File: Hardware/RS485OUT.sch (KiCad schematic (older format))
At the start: 14 parts

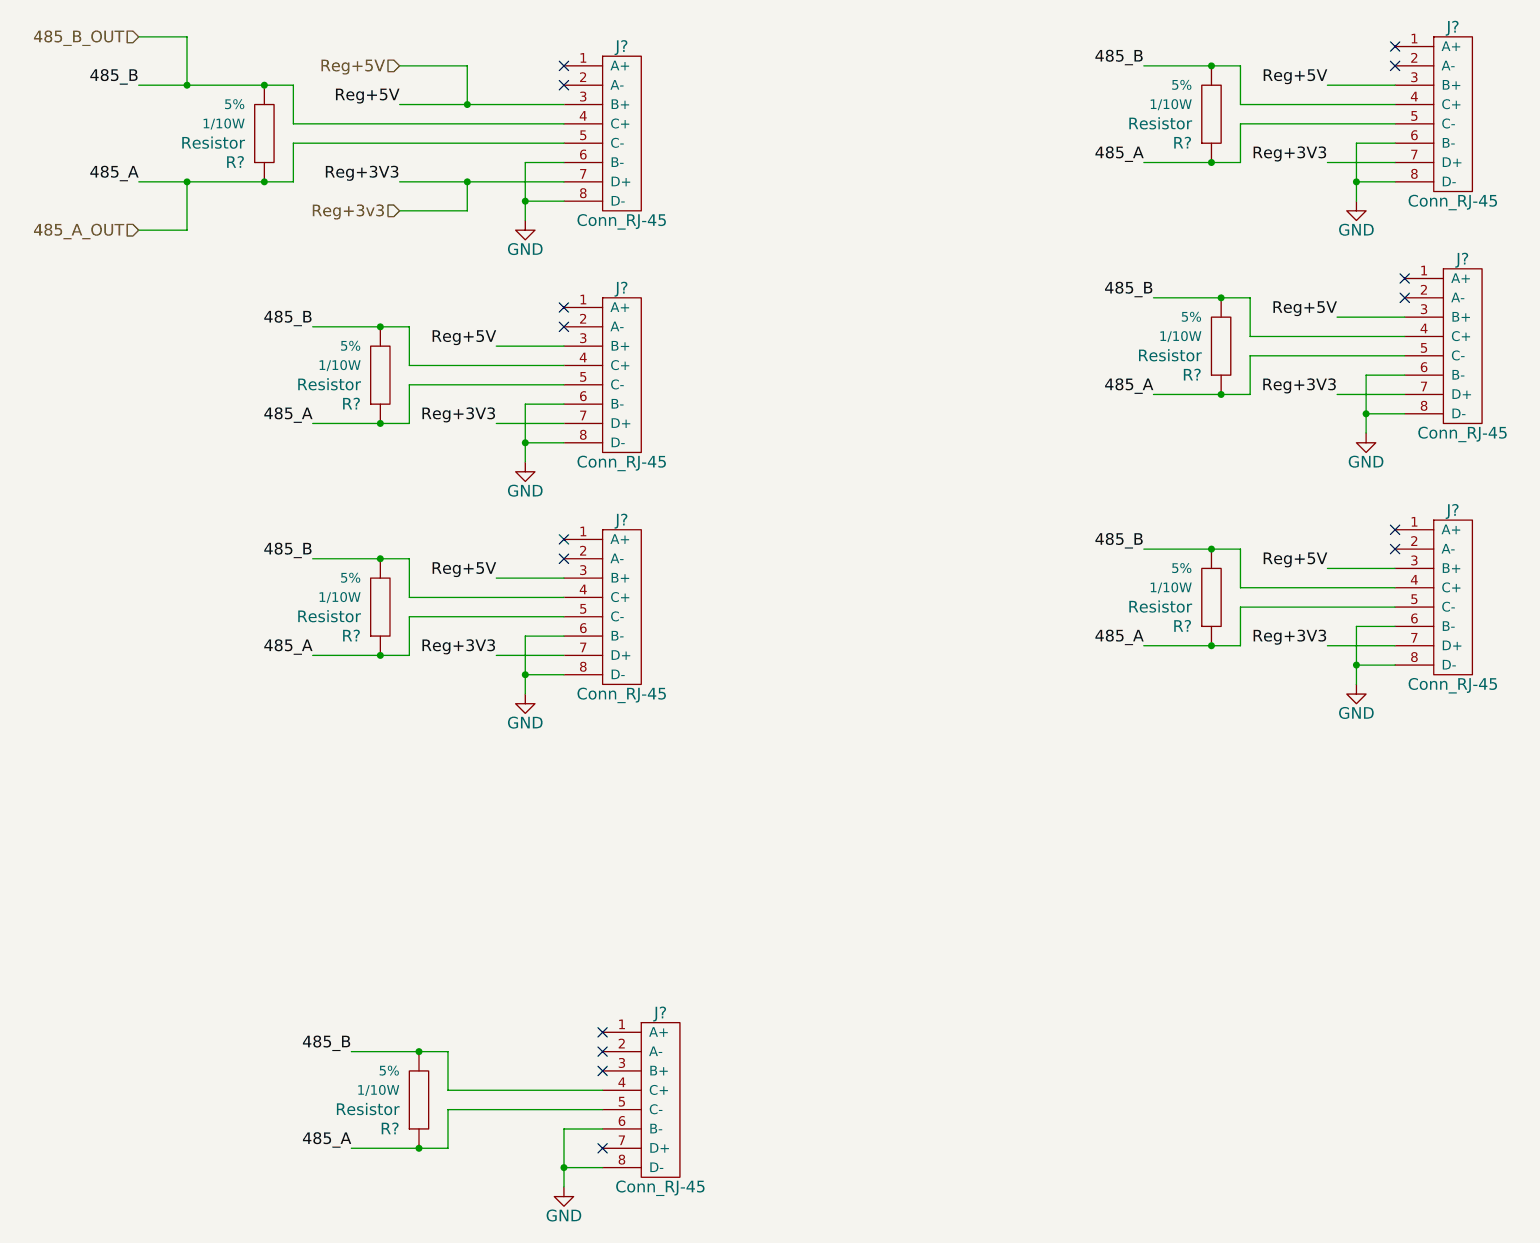
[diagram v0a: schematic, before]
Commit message: Add GPS Pads, potentiometer to INA125, 3v3 regulator always enabled, footprints created for GPS Pads and BTA, parts assigned
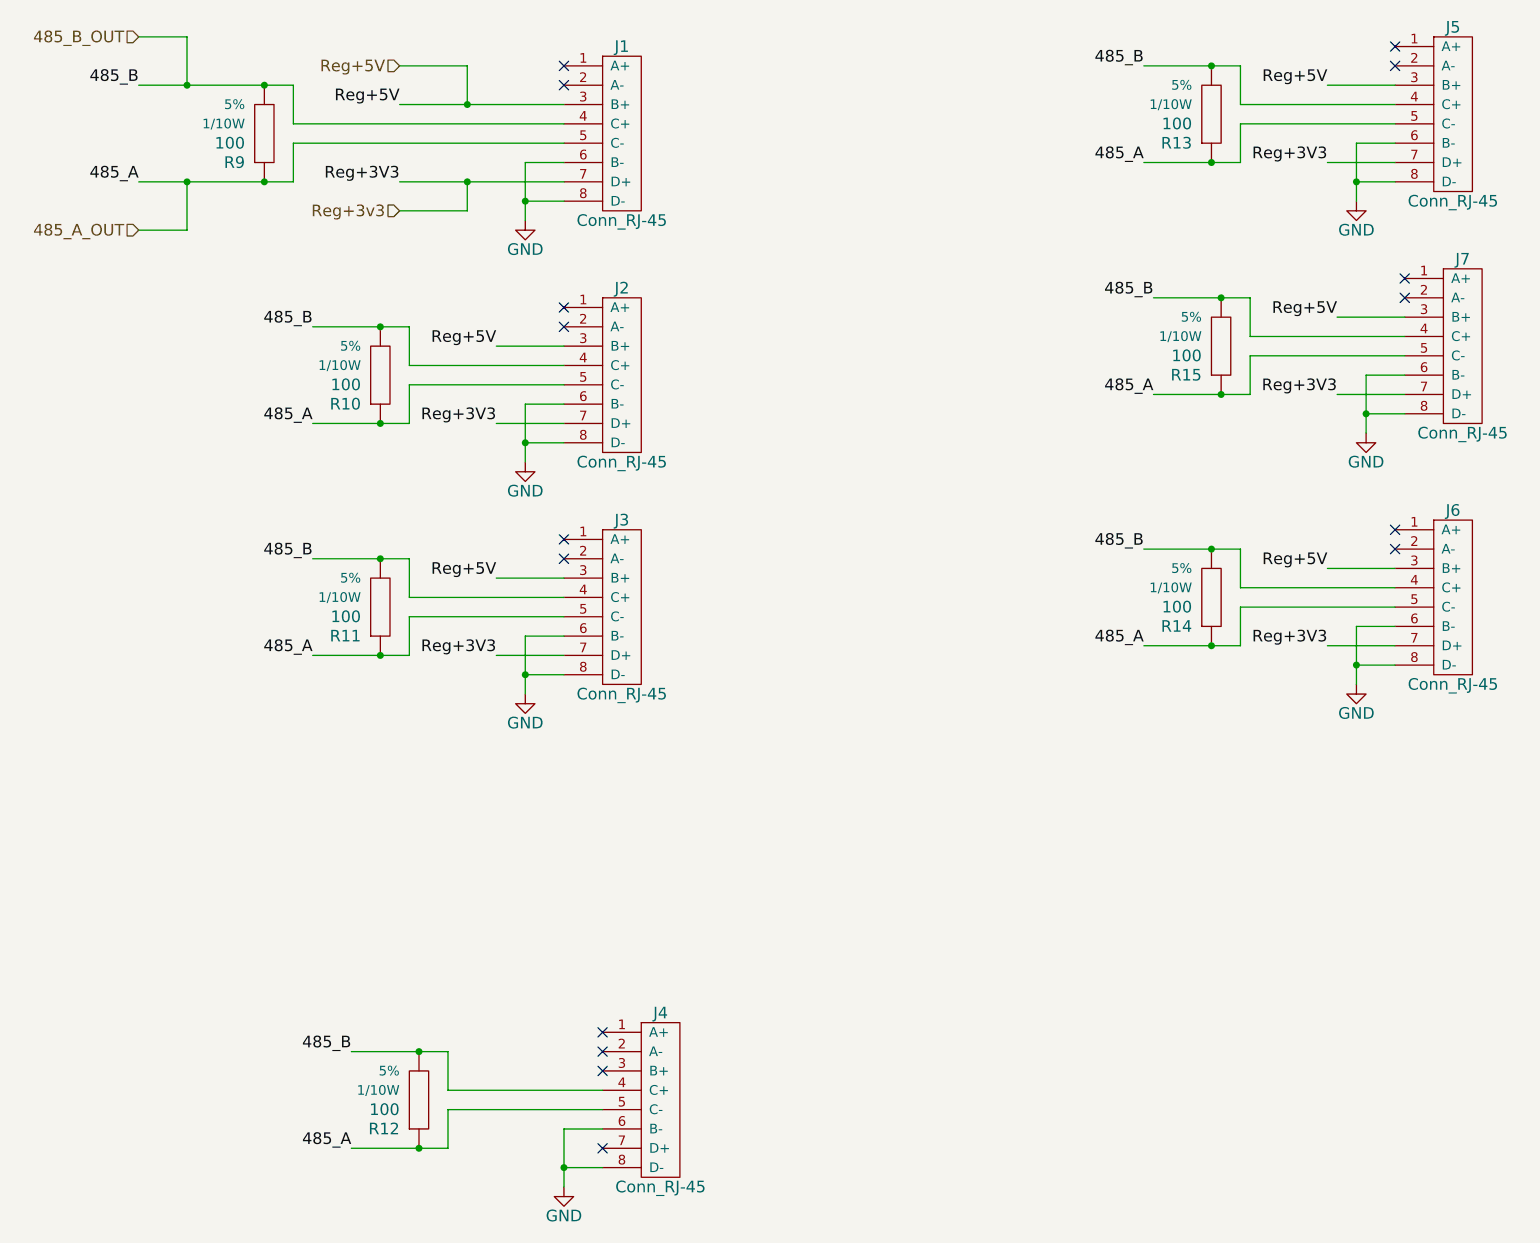
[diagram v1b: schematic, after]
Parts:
- J1, J2, J3, J4, J5, J6, J7: renamed from J?; footprint (none) -> MAVRIc:Molex_RJ45_0437438101
- R10, R11, R12, R13, R14, R15, R9: renamed from R?; value Resistor -> 100; footprint (none) -> Resistors_SMD:R_1206_HandSoldering
